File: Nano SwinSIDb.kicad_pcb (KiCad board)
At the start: 2 copper layers, 20.6 x 37.6 mm, 18 parts, among them J5 6PinConnector, U1 ATmega88PA-AU, U2 6581 Pins, U3 6581 Socket, X1 ECS-3225MV

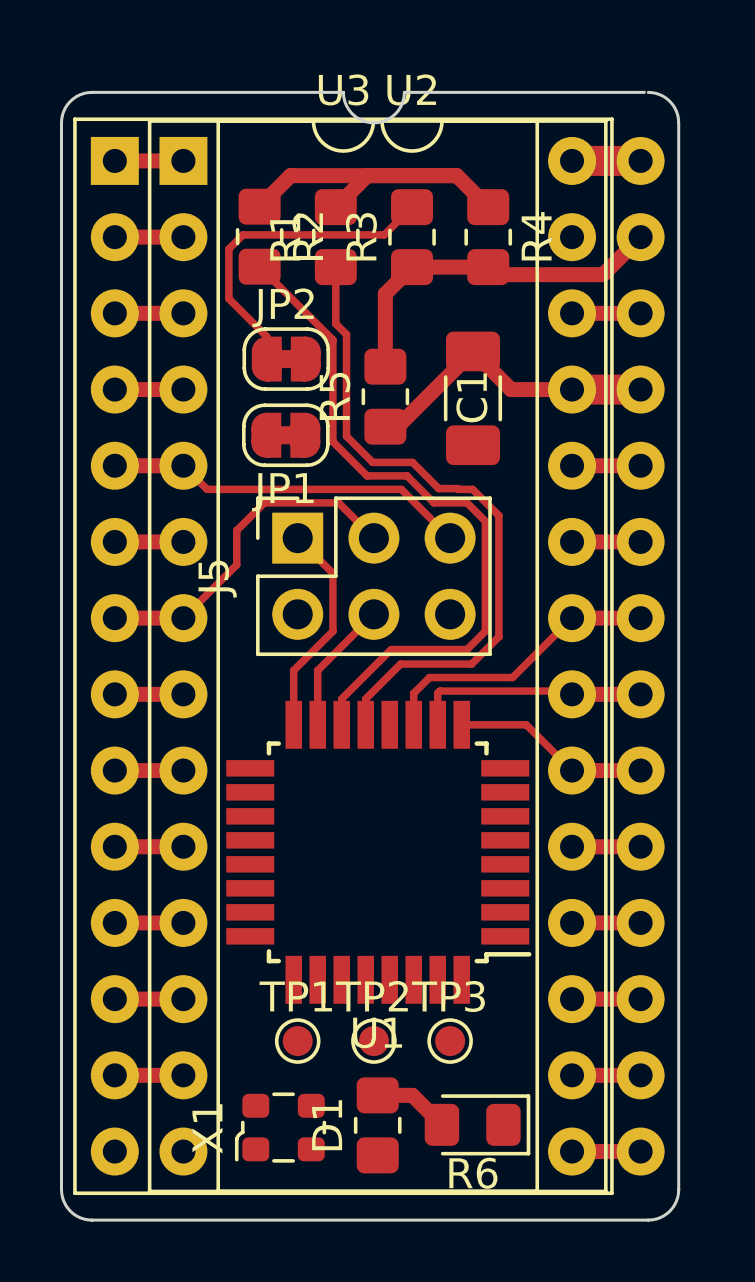
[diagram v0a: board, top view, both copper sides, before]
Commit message: First draft of PCB. Needs silkscreen work.
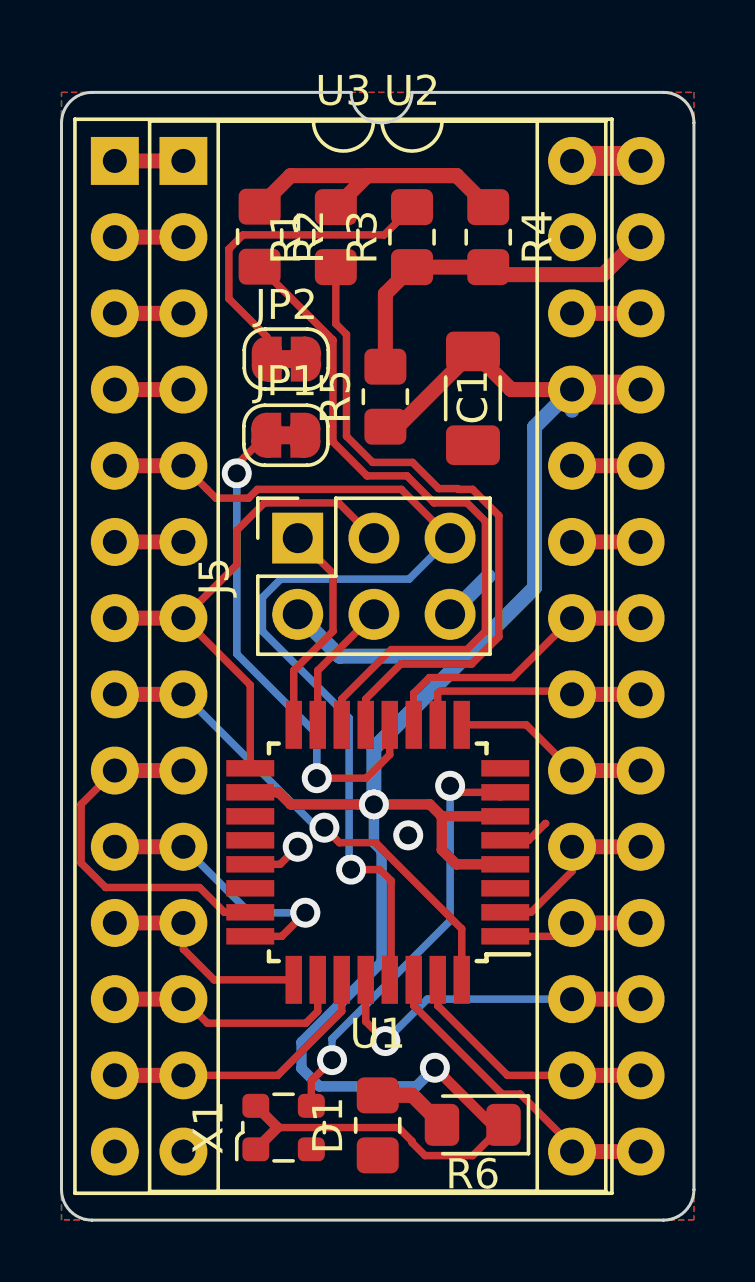
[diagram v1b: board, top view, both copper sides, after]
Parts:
- removed TP1, TP2, TP3: TestPoint, TestPoint:TestPoint_Pad_D1.0mm
- turned JP1 to 0 degrees
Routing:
- net VCC: track 10.1 -> 74.2 mm, vias 0 -> 2
- net /~RES~: track 12.2 -> 34.6 mm, vias 0 -> 1
- net /6581SEL: track 0.00 -> 16.7 mm, vias 0 -> 2
- net Net-(U1-Pad7): track 0.00 -> 14.8 mm, vias 0 -> 2
- net /~CS~: track 2.29 -> 16.5 mm, vias 0 -> 1
- net /A0: track 2.29 -> 12.2 mm
- net /D2: track 2.29 -> 11.4 mm, vias 0 -> 1
- net /D0: track 2.29 -> 10.5 mm
- net /A4: track 2.29 -> 9.50 mm
- net /A1: track 2.29 -> 9.42 mm, vias 0 -> 1
- net /D1: track 2.29 -> 8.59 mm
- net /A3: track 2.29 -> 8.31 mm
- net /R~W~: track 11.4 -> 17.3 mm
- net GND: track 0.00 -> 5.21 mm, vias 0 -> 2
- net /A2: track 2.29 -> 7.26 mm
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- added copper zone on B.Cu, net GND
- added copper zone on F.Cu, net GND
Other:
- board size 20.6 x 37.6 mm -> 21.1 x 37.6 mm

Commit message: Completed pcb design and gerber files for manufacture.
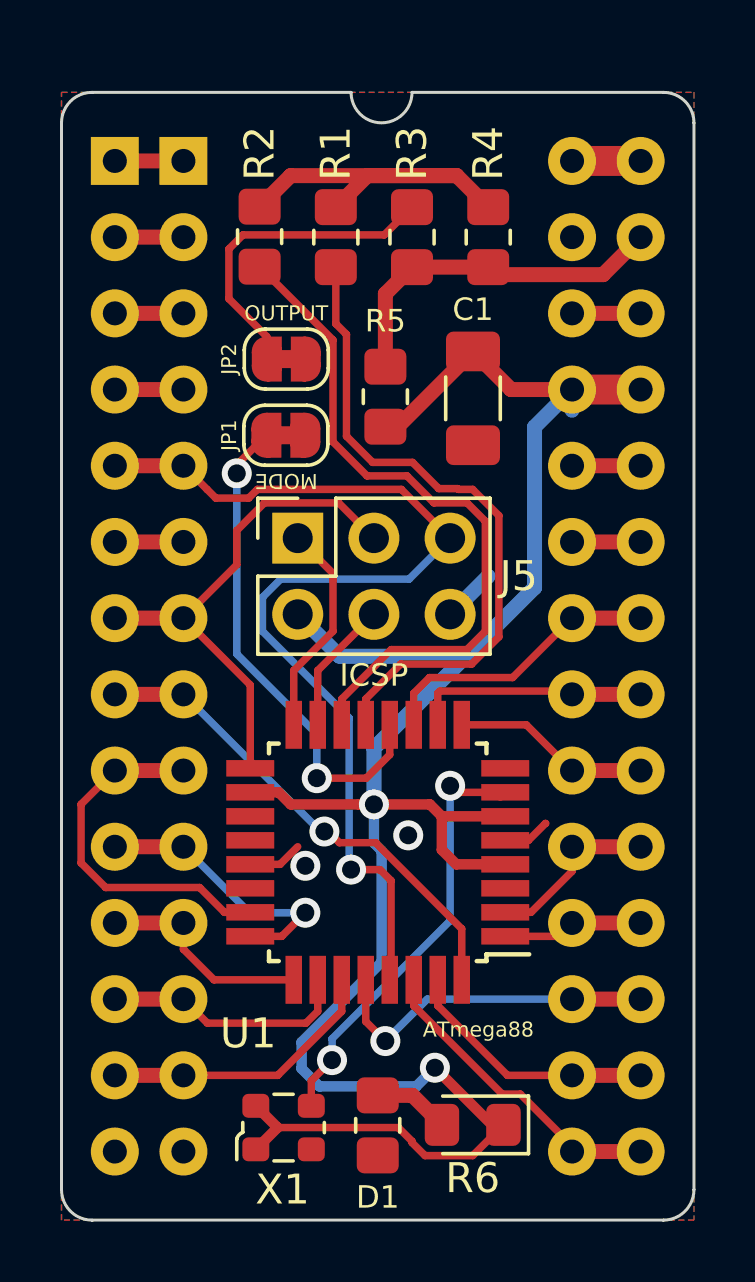
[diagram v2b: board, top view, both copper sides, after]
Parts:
- added REF**: OSHW-Logo2_7.3x6mm_SilkScreen, Symbol:OSHW-Logo2_7.3x6mm_SilkScreen, B.Cu at (102.9, 106.0)
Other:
- board text added: "ATmega88"
- board text added: "Board Pins 6851 Socket"
- board text added: "Created By: D Cooper Dalrymple 2021 dcdalrymple.com"
- board text added: "ICSP"
- board text added: "MODE"
- board text added: "OUTPUT"
- board text added: "Software & Hardware Info: dcdalrymple.com/NanoSwinSIDb-Piggyback"
- board text added: "SwinSID by Swinkels nano SwinSID by x1541"
